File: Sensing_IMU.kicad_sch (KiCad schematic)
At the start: 7 parts, among them U3202 BMI270

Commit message: Finished layout, only cleaning left
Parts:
- TP3201: renamed from TP2807; value INT1 -> IMU_INT1
- TP3202: renamed from TP2808; value INT2 -> IMU_INT2
- renumbered C2805 to C3201, C2806 to C3202, R812 to R3201, R813 to R3202, U3202 to U3201
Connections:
- net INT1 is gone; now on net IMU_INT1: TP3201.1
- net INT2 is gone; now on net IMU_INT2: TP3202.1
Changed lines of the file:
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@@
 			"AAAAAAAAAAAAAAAAAAAAAAAAAAAAAAAAAAAAAAAAAAAAAAAAAAAAAAAAAAAAAAAAAAAAAAAAAAAA"
 			"AAAAAAAAAAAAAAAAAAAAAAAAAAAAAAAAAAAAAAAAAAAAAAAAAAAAAAAAAAAAAAAAAAAAAAAAAAAA"
-			"AAAAAAAAAAAAAAAAAAAAAAAAAAAAAAAAAAAAAAAAAAAAAAAAAAAAAAAAAAAAAA=="
+			"AAAAAAAAAAAAAAAAAAAAAAAAAAAAAAAAAAAAAAAAAAAAAAAAAAAAAAAAAAAAAEppbDVvaS9iQ0NS"
+			"ZjltNHVlaUYvRE9qN2tyNnFTb1JmMlpabWJRT1NmcXBkU0grVE5LbGJYWFBiTml3UVZhc1dDRk5U"
+			"VTFBQ1lnQTRpK2dzQ2cxTndIRVgyNkVEQkFEQWNSZkRDbG1Xd1BpTHh1M3ZMMFFmOWtKSXYreXN5"
+			"dTdKL0pQajdoTDZhY3FWT0p2M0xoeE1uSGlSTDJDQzJ3VjA2MitvVWsvRlN2aXI4RE5IZW5RWFBF"
+			"WGJyQ0l2M0N6bzNKekFvZy9jMmIwaUpBQTRpL0NVRFdYaFBqVEJHVzVHZUl2SDFEa1h6NStaZlpH"
+			"L3JWTjI3WDBVOVY5OFl0ZmxMRmp4eUwrMm83SzZOTVFwWjlhSU9MUEtHWWF2N2xudU9JdnpLMkEr"
+			"QXN6TjZyT1JnRHhsNDBidlNJamdQaUxMRkNENVNEK0RHQlpiSXI0eXc4VCtaZWZZVmtqSVAvcWsv"
+			"WkIrcW5LRUgvMTg4bDZObFRwcDlhTCtNdWFlcnI5dU9JdjNPd1JmK0ZtUitYbUJCQi81c3pvRVNF"
+			"QnhGK0VvV291Q2ZHbkNjcHlNOFNmSGFESVB6c2N5eGdGK2RlYXNpL1NUMVdseE44MTExd2preVpO"
+			"YWwya2czZWgzK29ic3ZSVGNTUCtIR3o2d0tkRS9JVWJJT0l2M095bzNKd0E0cytjR1QwaUpJRDRp"
+			"ekJVelNVaC9qUkJXVzZHK0xNSEZQbG5qMlhSSXlILzNpRHNrL1JURlgzcFMxK1NNV1BHSVA1eS9n"
+			"RUlYZnFwNVNQK2NtNkNCTHNqL3NJTkhmRVhiblpVYms0QThXZk9qQjRSRWtEOFJSaXE1cElRZjVx"
+			"Z0xEZEQvTmtGaXZ5enk3UEkwVktYZjc1SlA1VTE0aS8vam85Qitpa0tpTC84ZXlHMUVSQi80U2FP"
+			"K0FzM095bzNKNEQ0TTJkR2p3aWE5OHd1QUFBWXAwbEVRVlFKSVA0aURGVnpTWWcvVFZDV215SCtM"
+			"QVA5LzNESVAvdE1peG94VmZubm8vUlRHU3Z4ZC9YVlY4dmt5Wk9MaWx4NzNCQnY5ZDIxYTVlc1c3"
+			"ZE96ampqREprNmRhbzBOVFZwcjllM2hvZy8zeEx4dng3RW4vOFpOYW9ROGRlSURPZGpKSUQ0aXpG"
+			"VjFtUk1BUEZuakN5YURvZy9OMUVpL29yaGp2d3JobXNSbzZZbS8zeVZmaXBieEYvMkhSNlQ5Rk1V"
+			"RUgvWjkwS3FQUkYvNFNhUCtBczNPeW8zSjRENE0yZEdqd2dKSVA0aURGVnpTWWcvVFZDV215SCtM"
+			"QU50TVJ6eXJ3VU16dzlUa1g4K1N6KzFSWll2WHk1WFhYVVZWL3daL25sUjBtLwBhAAAASAAAAHUA"
+			"AABBAAAAWQAAAHgAAAAwAAAAawAAADMAAAB1AAAAawAAAGUAAABuAAAALwAAAGkAAABsAAAAMAAA"
+			"AHcAAABVAAAAdQAAADgAAABpAAAAagAAAFQAAABkAAAAVgAAAHcAAABGAAAAZgAAAG4AAABoAAAA"
+			"aAAAAGsAAAAvAAAAUwAAAGgAAABtAAAAcgAAAEgAAABMAAAANgAAAEkAAAA5AAAAdQAAAGoAAABJ"
+			"AAAARgAAAHoAAABNAAAAWAAAAFgAAABmAAAAbAAAAGUAAABrAAAAeAAAADkAAAB2AAAAaQAAAHAA"
+			"AABnAAAASwAAAFAAAABTAAAARgAAAGQAAABFAAAAMAAAAEYAAABYAAAAegAAAEgAAABUAAAAQQAA"
+			"ACsAAABhAAAAZgAAAGoAAABKAAAATgAAADIAAABNAAAAagAAAFkAAABMAAAAZAAAAE0AAAAyAAAA"
+			"dwAAAEEAAAA2AAAAZAAAAHAAAABOAAAAawAAAEcAAABEAAAASgAAAEEAAABOAAAAMwAAACsAAABq"
+			"AAAASwAAAFIAAAAxAAAANwAAADgAAABBAAAAVgAAAHcAAAB6AAAAaAAAAFIAAABxAAAAYgAAAEEA"
+			"AAB4AAAAcgAAAHcAAABvAAAATAAAADAAAABCAAAAQQAAAE0AAABCAAAASwAAAEIAAABNAAAAWgAA"
+			"ADYAAABJAAAAZwAAAG4AAAB3AAAAMAAAAEoAAABaAAAAawAAAEkAAABPAAAAYwAAAEEAAAAyAAAA"
+			"eAAAAG0AAABUAAAARwAAAHYAAABXAAAAaQAAAGEAAAA3AAAATAAAAHYAAABXAAAANAAAAGUAAABO"
+			"AAAAVQAAAHYAAABXAAAANwAAAFYAAABPAAAAbwAAAEYAAABTAAAASgAAAFgAAABEAAAARwAAAHoA"
+			"AABtAAAAMAAAADMAAAA5AAAASQAAAFUAAABDAAAAUwAAAHkAAABJAAAAZQAAADIAAABuAAAAQQAA"
+			"AG8AAABtAAAATwAAADYAAABzAAAALwAAAG4AAABOAAAAUgAAAE8AAAAzAAAAawAAAEkAAABWAAAA"
+			"VQAAADUAAAAzAAAAegAAAEIAAABqAAAANwAAADMAAABTAAAAQwAAAFgAAAAyAAAAQgAAAFEAAAAz"
+			"AAAAZAAAAHIAAABPAAAAWAAAAHQAAAB1AAAAaQAAAGoAAABUAAAAOQAAAHQAAABaAAAAegAAACsA"
+			"AAAyAAAATQAAAG4AAABiAAAAWAAAAEoAAABRAAAAQgAAACsAAABvAAAAcwAAAGYAAAAzAAAAdgAA"
+			"AHUAAAB3AAAAOQAAAHoAAABMAAAAQgAAAFAAAABnAAAARgAAADgAAAA3AAAAVw=="
 		)
 	)
@@
 		)
 	)
-	(label "INT2"
+	(label "IMU_INT2"
 		(at 22.86 97.79 0)
 		(effects
@@
 		)
 	)
-	(label "INT1"
+	(label "IMU_INT1"
 		(at 22.86 92.71 0)
 		(effects
@@
 		(on_board yes)
 		(dnp no)
-		(property "Reference" "R812"
+		(property "Reference" "R3201"
 			(at 118.618 86.868 0)
 			(effects
@@
 			(project "Plume"
 				(path "/0650c7a8-acba-429c-9f8e-eec0baf0bc1c/fede4c36-00cc-4d3d-b71c-5243ba232202/107f1a8c-fcbf-4d4a-9f6a-e2cb21670a9f"
-					(reference "R812")
+					(reference "R3201")
 					(unit 1)
 				)
@@
 		(dnp no)
 		(fields_autoplaced yes)
-		(property "Reference" "#PWR0706"
+		(property "Reference" "#PWR03202"
 			(at 154.94 93.98 0)
 			(effects
@@
 			(project "Plume"
 				(path "/0650c7a8-acba-429c-9f8e-eec0baf0bc1c/fede4c36-00cc-4d3d-b71c-5243ba232202/107f1a8c-fcbf-4d4a-9f6a-e2cb21670a9f"
-					(reference "#PWR0706")
+					(reference "#PWR03202")
 					(unit 1)
 				)
@@
 		(dnp no)
 		(fields_autoplaced yes)
-		(property "Reference" "#PWR0704"
+		(property "Reference" "#PWR03204"
 			(at 151.13 121.92 0)
 			(effects
@@
 			(project "Plume"
 				(path "/0650c7a8-acba-429c-9f8e-eec0baf0bc1c/fede4c36-00cc-4d3d-b71c-5243ba232202/107f1a8c-fcbf-4d4a-9f6a-e2cb21670a9f"
-					(reference "#PWR0704")
+					(reference "#PWR03204")
 					(unit 1)
 				)
@@
 		(on_board yes)
 		(dnp no)
-		(property "Reference" "TP2807"
+		(property "Reference" "TP3201"
 			(at 43.18 92.71 90)
 			(effects
@@
 			)
 		)
-		(property "Value" "INT1"
+		(property "Value" "IMU_INT1"
 			(at 50.546 92.71 90)
 			(effects
@@
 			(project "Plume"
 				(path "/0650c7a8-acba-429c-9f8e-eec0baf0bc1c/fede4c36-00cc-4d3d-b71c-5243ba232202/107f1a8c-fcbf-4d4a-9f6a-e2cb21670a9f"
-					(reference "TP2807")
+					(reference "TP3201")
 					(unit 1)
 				)
@@
 		(dnp no)
 		(fields_autoplaced yes)
-		(property "Reference" "#PWR0707"
+		(property "Reference" "#PWR03203"
 			(at 135.89 100.33 0)
 			(effects
@@
 			(project "Plume"
 				(path "/0650c7a8-acba-429c-9f8e-eec0baf0bc1c/fede4c36-00cc-4d3d-b71c-5243ba232202/107f1a8c-fcbf-4d4a-9f6a-e2cb21670a9f"
-					(reference "#PWR0707")
+					(reference "#PWR03203")
 					(unit 1)
 				)
@@
 		(dnp no)
 		(fields_autoplaced yes)
-		(property "Reference" "#PWR0705"
+		(property "Reference" "#PWR03201"
 			(at 147.32 93.98 0)
 			(effects
@@
 			(project "Plume"
 				(path "/0650c7a8-acba-429c-9f8e-eec0baf0bc1c/fede4c36-00cc-4d3d-b71c-5243ba232202/107f1a8c-fcbf-4d4a-9f6a-e2cb21670a9f"
-					(reference "#PWR0705")
+					(reference "#PWR03201")
 					(unit 1)
 				)
@@
 		(on_board yes)
 		(dnp no)
-		(property "Reference" "R813"
+		(property "Reference" "R3202"
 			(at 128.778 86.868 0)
 			(effects
@@
 			(project "Plume"
 				(path "/0650c7a8-acba-429c-9f8e-eec0baf0bc1c/fede4c36-00cc-4d3d-b71c-5243ba232202/107f1a8c-fcbf-4d4a-9f6a-e2cb21670a9f"
-					(reference "R813")
+					(reference "R3202")
 					(unit 1)
 				)
@@
 		(on_board yes)
 		(dnp no)
-		(property "Reference" "C2805"
+		(property "Reference" "C3201"
 			(at 144.78 82.55 0)
 			(effects
@@
 			(project "Plume"
 				(path "/0650c7a8-acba-429c-9f8e-eec0baf0bc1c/fede4c36-00cc-4d3d-b71c-5243ba232202/107f1a8c-fcbf-4d4a-9f6a-e2cb21670a9f"
-					(reference "C2805")
+					(reference "C3201")
 					(unit 1)
 				)
@@
 		(on_board yes)
 		(dnp no)
-		(property "Reference" "U3202"
+		(property "Reference" "U3201"
 			(at 142.494 92.71 0)
 			(effects
@@
 			(project ""
 				(path "/0650c7a8-acba-429c-9f8e-eec0baf0bc1c/fede4c36-00cc-4d3d-b71c-5243ba232202/107f1a8c-fcbf-4d4a-9f6a-e2cb21670a9f"
-					(reference "U3202")
+					(reference "U3201")
 					(unit 1)
 				)
@@
 		(on_board yes)
 		(dnp no)
-		(property "Reference" "TP2808"
+		(property "Reference" "TP3202"
 			(at 43.18 97.79 90)
 			(effects
@@
 			)
 		)
-		(property "Value" "INT2"
+		(property "Value" "IMU_INT2"
 			(at 50.546 97.79 90)
 			(effects
@@
 			(project "Plume"
 				(path "/0650c7a8-acba-429c-9f8e-eec0baf0bc1c/fede4c36-00cc-4d3d-b71c-5243ba232202/107f1a8c-fcbf-4d4a-9f6a-e2cb21670a9f"
-					(reference "TP2808")
+					(reference "TP3202")
 					(unit 1)
 				)
@@
 		(on_board yes)
 		(dnp no)
-		(property "Reference" "C2806"
+		(property "Reference" "C3202"
 			(at 157.48 82.55 0)
 			(effects
@@
 			(project "Plume"
 				(path "/0650c7a8-acba-429c-9f8e-eec0baf0bc1c/fede4c36-00cc-4d3d-b71c-5243ba232202/107f1a8c-fcbf-4d4a-9f6a-e2cb21670a9f"
-					(reference "C2806")
+					(reference "C3202")
 					(unit 1)
 				)

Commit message: Finished cleaning routing, removed errors, cleaned shematics, added pictures and other improvements
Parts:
- renumbered C3201 to C1001, C3202 to C1002, R3201 to R1001, R3202 to R1002, TP3201 to TP1001, TP3202 to TP1002, U3201 to U1001
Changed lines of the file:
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@@
 			"AAAAZAAAAHIAAABPAAAAWAAAAHQAAAB1AAAAaQAAAGoAAABUAAAAOQAAAHQAAABaAAAAegAAACsA"
 			"AAAyAAAATQAAAG4AAABiAAAAWAAAAEoAAABRAAAAQgAAACsAAABvAAAAcwAAAGYAAAAzAAAAdgAA"
-			"AHUAAAB3AAAAOQAAAHoAAABMAAAAQgAAAFAAAABnAAAARgAAADgAAAA3AAAAVw=="
+			"AHUAAAB3AAAAOQAAAHoAAABMAAAAQgAAAFAAAABnAAAARgAAADgAAAA3AAAAVwAAADcAAABLAAAA"
+			"cwAAAFEAAABqAAAAZwAAAGMAAABCAAAAQgAAAEIAAABBAAAAQQAAAEEAAABFAAAARQAAAEUAAABF"
+			"AAAAZwAAAG8AAABRAAAASgAAAHMAAABsAAAASQAAAFEAAABzAAAAVAAAAEUAAABVAAAAQQAAAEEA"
+			"AABBAAAAUQAAAFEAAABRAAAAUQAAAEEAAABBAAAAQgAAAEIAAABDAAAAcAAAAFoAAABJAAAATAAA"
+			"AFEAAAA3AAAAcQAAAHkAAAAyAAAAZwAAAHQAAABKAAAATAAAAFAAAABoAAAAOAAAADAAAABoAAAA"
+			"ZwAAAEEAAABBAAAAQwAAAEMAAABDAAAAQwAAAEEAAABBAAAAQQAAAEkAAABJAAAASQAAAEkAAABB"
+			"AAAAQQAAAEEAAABnAAAAZwAAAGcAAABnAAAAQQAAAEEAAABDAAAAQwAAAEMAAABDAAAAQQAAAEEA"
+			"AABBAAAASQAAAEkAAABJAAAASQAAAEEAAABBAAAAQQAAAGcAAABnAAAAZwAAAGcAAABBAAAAQQAA"
+			"AEMAAABDAAAAQwAAAEMAAABBAAAAQQAAAEEAAABJAAAASQAAAEkAAABJAAAAQQAAAEEAAABBAAAA"
+			"ZwAAAGcAAABnAAAAZwAAAEEAAABBAAAAQwAAAEMAAABGAAAAUgAAAFEAAABnAAAASQAAAEQAAABT"
+			"AAAAQwAAAHMAAABLAAAAeAAAAEcAAABnAAAASQAAAEkAAABJAAAASQAAAEEAAABBAAAAQQAAAGcA"
+			"AABnAAAAZwAAAGcAAABBAAAAQQAAAEMAAABDAAAAQwAAAEMAAABBAAAAQQAAAEEAAABJAAAASQAA"
+			"AEkAAABJAAAAQQAAAEEAAABBAAAAZwAAAGcAAABnAAAAZwAAAEEAAABBAAAAQwAAAEMAAABDAAAA"
+			"QwAAAEEAAABBAAAAQQAAAEkAAABJAAAASQAAAEkAAABBAAAAQQAAAEEAAABnAAAAZwAAAGcAAABn"
+			"AAAAQQAAAEEAAABDAAAAQwAAAEMAAABDAAAAQQAAAEEAAABBAAAASQAAAEkAAABJAAAASgAAAEEA"
+			"AAB2AAAAQQAAAHQAAABVAAAAVwAAAFUAAABMAAAAcgAAAE8AAABiAAAAOAAAAHYAAAB5AAAAeAAA"
+			"AFoAAABEAAAAegAAAFEAAABBAAAAQQAAAEIAAABCAAAARAAAAEkAAAB1AAAAOAAAAFAAAAAxAAAA"
+			"cQAAAE4AAABmAAAAdwAAACsAAAB1AAAASAAAAFoAAABtAAAAbgAAAEoAAABvAAAAZAAAAEkAAABJ"
+			"AAAAQQAAAEEAAABBAAAAZwAAAGcAAABnAAAAZwAAAEEAAABBAAAAQwAAAEMAAA=="
 		)
 	)
@@
 		(on_board yes)
 		(dnp no)
-		(property "Reference" "R3201"
+		(property "Reference" "R1001"
 			(at 118.618 86.868 0)
 			(effects
@@
 			(project "Plume"
 				(path "/0650c7a8-acba-429c-9f8e-eec0baf0bc1c/fede4c36-00cc-4d3d-b71c-5243ba232202/107f1a8c-fcbf-4d4a-9f6a-e2cb21670a9f"
-					(reference "R3201")
+					(reference "R1001")
 					(unit 1)
 				)
@@
 		(dnp no)
 		(fields_autoplaced yes)
-		(property "Reference" "#PWR03202"
+		(property "Reference" "#PWR01002"
 			(at 154.94 93.98 0)
 			(effects
@@
 			(project "Plume"
 				(path "/0650c7a8-acba-429c-9f8e-eec0baf0bc1c/fede4c36-00cc-4d3d-b71c-5243ba232202/107f1a8c-fcbf-4d4a-9f6a-e2cb21670a9f"
-					(reference "#PWR03202")
+					(reference "#PWR01002")
 					(unit 1)
 				)
@@
 		(dnp no)
 		(fields_autoplaced yes)
-		(property "Reference" "#PWR03204"
+		(property "Reference" "#PWR01004"
 			(at 151.13 121.92 0)
 			(effects
@@
 			(project "Plume"
 				(path "/0650c7a8-acba-429c-9f8e-eec0baf0bc1c/fede4c36-00cc-4d3d-b71c-5243ba232202/107f1a8c-fcbf-4d4a-9f6a-e2cb21670a9f"
-					(reference "#PWR03204")
+					(reference "#PWR01004")
 					(unit 1)
 				)
@@
 		(on_board yes)
 		(dnp no)
-		(property "Reference" "TP3201"
+		(property "Reference" "TP1001"
 			(at 43.18 92.71 90)
 			(effects
@@
 			(project "Plume"
 				(path "/0650c7a8-acba-429c-9f8e-eec0baf0bc1c/fede4c36-00cc-4d3d-b71c-5243ba232202/107f1a8c-fcbf-4d4a-9f6a-e2cb21670a9f"
-					(reference "TP3201")
+					(reference "TP1001")
 					(unit 1)
 				)
@@
 		(dnp no)
 		(fields_autoplaced yes)
-		(property "Reference" "#PWR03203"
+		(property "Reference" "#PWR01003"
 			(at 135.89 100.33 0)
 			(effects
@@
 			(project "Plume"
 				(path "/0650c7a8-acba-429c-9f8e-eec0baf0bc1c/fede4c36-00cc-4d3d-b71c-5243ba232202/107f1a8c-fcbf-4d4a-9f6a-e2cb21670a9f"
-					(reference "#PWR03203")
+					(reference "#PWR01003")
 					(unit 1)
 				)
@@
 		(dnp no)
 		(fields_autoplaced yes)
-		(property "Reference" "#PWR03201"
+		(property "Reference" "#PWR01001"
 			(at 147.32 93.98 0)
 			(effects
@@
 			(project "Plume"
 				(path "/0650c7a8-acba-429c-9f8e-eec0baf0bc1c/fede4c36-00cc-4d3d-b71c-5243ba232202/107f1a8c-fcbf-4d4a-9f6a-e2cb21670a9f"
-					(reference "#PWR03201")
+					(reference "#PWR01001")
 					(unit 1)
 				)
@@
 		(on_board yes)
 		(dnp no)
-		(property "Reference" "R3202"
+		(property "Reference" "R1002"
 			(at 128.778 86.868 0)
 			(effects
@@
 			(project "Plume"
 				(path "/0650c7a8-acba-429c-9f8e-eec0baf0bc1c/fede4c36-00cc-4d3d-b71c-5243ba232202/107f1a8c-fcbf-4d4a-9f6a-e2cb21670a9f"
-					(reference "R3202")
+					(reference "R1002")
 					(unit 1)
 				)
@@
 		(on_board yes)
 		(dnp no)
-		(property "Reference" "C3201"
+		(property "Reference" "C1001"
 			(at 144.78 82.55 0)
 			(effects
@@
 			(project "Plume"
 				(path "/0650c7a8-acba-429c-9f8e-eec0baf0bc1c/fede4c36-00cc-4d3d-b71c-5243ba232202/107f1a8c-fcbf-4d4a-9f6a-e2cb21670a9f"
-					(reference "C3201")
+					(reference "C1001")
 					(unit 1)
 				)
@@
 		(on_board yes)
 		(dnp no)
-		(property "Reference" "U3201"
+		(property "Reference" "U1001"
 			(at 142.494 92.71 0)
 			(effects
@@
 			(project ""
 				(path "/0650c7a8-acba-429c-9f8e-eec0baf0bc1c/fede4c36-00cc-4d3d-b71c-5243ba232202/107f1a8c-fcbf-4d4a-9f6a-e2cb21670a9f"
-					(reference "U3201")
+					(reference "U1001")
 					(unit 1)
 				)
@@
 		(on_board yes)
 		(dnp no)
-		(property "Reference" "TP3202"
+		(property "Reference" "TP1002"
 			(at 43.18 97.79 90)
 			(effects
@@
 			(project "Plume"
 				(path "/0650c7a8-acba-429c-9f8e-eec0baf0bc1c/fede4c36-00cc-4d3d-b71c-5243ba232202/107f1a8c-fcbf-4d4a-9f6a-e2cb21670a9f"
-					(reference "TP3202")
+					(reference "TP1002")
 					(unit 1)
 				)
@@
 		(on_board yes)
 		(dnp no)
-		(property "Reference" "C3202"
+		(property "Reference" "C1002"
 			(at 157.48 82.55 0)
 			(effects
@@
 			(project "Plume"
 				(path "/0650c7a8-acba-429c-9f8e-eec0baf0bc1c/fede4c36-00cc-4d3d-b71c-5243ba232202/107f1a8c-fcbf-4d4a-9f6a-e2cb21670a9f"
-					(reference "C3202")
+					(reference "C1002")
 					(unit 1)
 				)

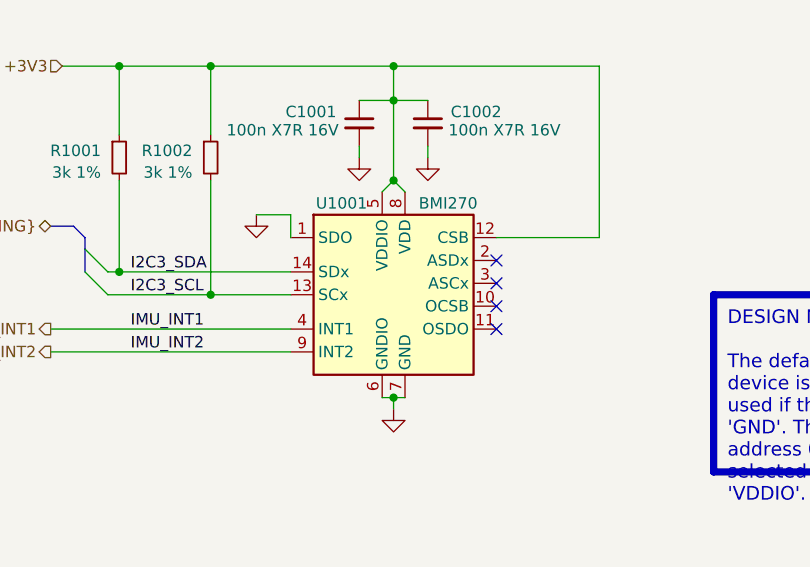
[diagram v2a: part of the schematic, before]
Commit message: Added PCB frame
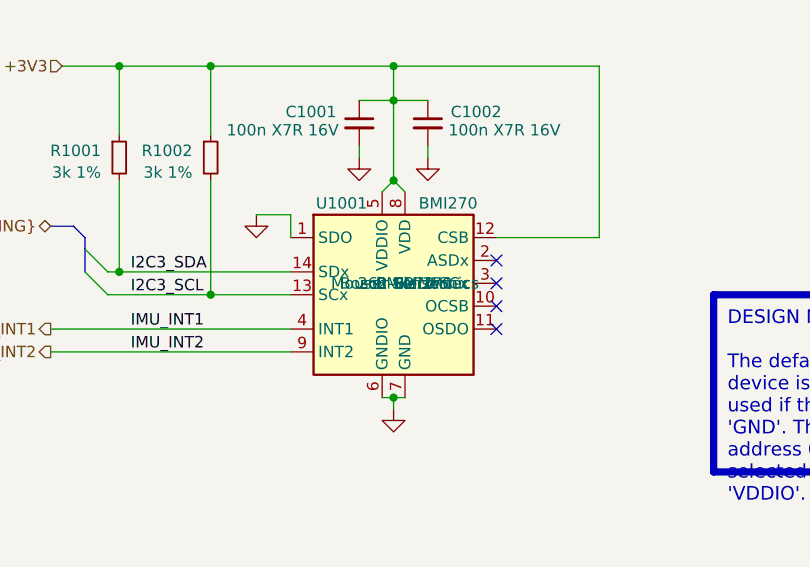
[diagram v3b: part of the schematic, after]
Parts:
- U1001: Manufacturer (none) -> Bosch Sensortec; Manufacturer Part Number (none) -> BMI270; Supplier (none) -> Mouser Electronics; Supplier Part Number (none) -> 262-BMI270
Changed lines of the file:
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@@
 			"AFoAAABEAAAAegAAAFEAAABBAAAAQQAAAEIAAABCAAAARAAAAEkAAAB1AAAAOAAAAFAAAAAxAAAA"
 			"cQAAAE4AAABmAAAAdwAAACsAAAB1AAAASAAAAFoAAABtAAAAbgAAAEoAAABvAAAAZAAAAEkAAABJ"
-			"AAAAQQAAAEEAAABBAAAAZwAAAGcAAABnAAAAZwAAAEEAAABBAAAAQwAAAEMAAA=="
+			"AAAAQQAAAEEAAABBAAAAZwAAAGcAAABnAAAAZwAAAEEAAABBAAAAQwAAAEMAAAAAAAAAAAAAAAAA"
+			"AAAAAAAAAAAAAAAAAAAAAAAAAAAAAAAAAAAAAAAAAAAAAAAAAAAAAAAAAAAAAAAAAAAAAAAAAAAA"
+			"AAAAAAAAAAAAAAAAAAAAAAAAAAAAAAAAAAAAAAAAAAAAAAAAAAAAAAAAAAAAAAAAAAAAAAAAAAAA"
+			"AAAAAAAAAAAAAAAAAAAAAAAAAAAAAAAAAAAAAAAAAAAAAAAAAAAAAAAAAAAAAAAAAAAAAAAAAAAA"
+			"AAAAAAAAAAAAAAAAAAAAAAAAAAAAAAAAAAAAAAAAAAAAAAAAAAAAAAAAAAAAAAAAAAAAAAAAAAAA"
+			"AAAAAAAAAAAAAAAAAAAAAAAAAAAAAAAAAAAAAAAAAAAAAAAAAAAAAAAAAAAAAAAAAAAAAAAAAAAA"
+			"AAAAAAAAAAAAAAAAAAAAAAAAAAAAAAAAAAAAAAAAAAAAAAAAAAAAAAAAAAAAAAAAAAAAAAAAAAAA"
+			"AAAAAAAAAAAAAAAAAAAAAAAAAAAAAAAAAAAAAAAAAAAAAAAAAAAAAAAAAAAAAAAAAAAAAAAAAAAA"
+			"AAAAAAAAAAAAAAAAAAAAAAAAAAAAAAAAAAAAAAAAAAAAAAAAAAAAAAAAAAAAAAAAAAAAAAAAAAAA"
+			"AAAAAAAAAAAAAAAAAAAAAAAAAAAAAAAAAAAAAAAAAAAAAAAAAAAAAAAAAAAAAAAAAAAAAAAAAAAA"
+			"AAAAAAAAAAAAAAAAAAAAAAAAAAAAAAAAAAAAAAAAAAAAAAAAAAAAAAAAAAAAAAAAAAAAAAAAAAAA"
+			"AAAAAAAAAAAAAAAAAAAAAAAAAAAAAAAAAAAAAAAAAAAAAAAAAAAAAAAAAAAAAAAAAAAAAAAAAAAA"
+			"AAAAAAAAAAAAAAAAAAAAAAAAAAAAAAAAAAAAAAAAAAAAAAAAAAAAAAAAAAAAAAAAAAAAAAAAAAAA"
+			"AAAAAAAAAAAAAAAAAAAAAAAAAAAAAAAAAAAAAAAAAAAAAAAAAAAAAAAAAAAAAAAAAAAAAAAAAAAA"
+			"AAAAAAAAAAAAAAAAAAAAAAAAAAAAAAAAAAAAAAAAAAAAAAAAAAAAAAAAAAAAAAAAAAAAAAAAAAAA"
+			"AAAAAAAAAAAAAAAAAAAAAAAAAAAAAAAAAAAAAAAAAAAAAAAAAAAAAAAAAAAAAAAAAAAAAAAAAAAA"
+			"AAAAAAAAAAAAAAAAAAAAAAAAAAAAAAAAAAAAAAAAAAAAAAAAAAAAAAAAAAAAAAAAAAAAAAAAAAAA"
+			"AAAAAAAAAAAAAAAAAAAAAAAAAAAAAAAAAAAAAAAAAAAAAAAAAAAAAAAAAAAAAAAAAAAAAAAAAAAA"
+			"AAAAAAAAAAAAAAAAAAAAAAAAAAAAAAAAAAAAAAAAAAAAAAAAAAAAAAAAAAAAAAAAADgAAABGAAAA"
+			"NAAAAFcAAABNAAAANwAAAGIAAABLAAAAagAAADYAAABVAAAAUQAAAGYAAABhAAAATwAAAFoAAAAy"
+			"AAAAQgAAACsAAAAwAAAAcAAAAGsAAAB4AAAAUQAAAGQAAABkAAAATgAAAEQAAABxAAAAYQAAAHQA"
+			"AAA3AAAALwAAAGkAAAB4AAAARQAAAFYAAABIAAAAMgAAAHkAAABiAAAAYQAAAEQAAAA2AAAAQQAA"
+			"AFMAAAB1AAAAZQAAAFAAAAB3AAAAUgAAAFgAAABnAAAAOAAAAHQAAABhAAAATgAAAEQAAAA4AAAA"
+			"awAAAGEAAAA3AAAAMAAAAEoAAABkAAAASAAAAHYAAABhAAAAWQAAADYAAAA5AAAAagAAAGYAAAAz"
+			"AAAATwAAAEUAAABNAAAATwAAAG0AAABpAAAAegAAAEEAAABnAAAAYgAAAHIAAABVAAAANwAAAFQA"
+			"AAA1AAAAbgAAAGoAAABSAAAALwAAAGEAAABkAAAAWQAAADYAAABlAAAAZQAAADgAAABrAAAANgAA"
+			"AGUAAABxAAAATgAAAEgAAABkAAAAUAAAAFgAAAB4AAAAYQAAAGEAAAB2AAAAbwAAAFYAAAAvAAAA"
+			"MAAAAGMAAAB5AAAAVAAAAG8AAABnAAAAYgAAAFkAAABDAAAATwAAAGYAAABCAAAAeQAAAHUAAAA0"
+			"AAAAOQAAAG8AAAB6AAAAMAAAAE4AAABPAAAAMwAAAHkAAAB2AAAAQgAAAE4AAABaAAAAcAAAAEUA"
+			"AABLAAAANQAAAGQAAABqAAAAaQAAADkAAABoAAAAbQAAAHQAAABoAAAAMQAAADkAAAByAAAAMwAA"
+			"AGUAAABoAAAATAAAACsAAAA2AAAASAAAAEYAAAB1AAAAWQAAAHQAAABzAAAAUwAAAFQAAABNAAAA"
+			"ZQAAAEcAAABTAAAAdgAAAEcAAAAyAAAAZgAAAFYAAABUAAAAQQAAAFgAAABSAAAAegAAAHYAAABO"
+			"AAAAZAAAAG8AAABnAAAAagAAAFkAAABVAAAAMQAAAGUAAABIAAAAcwAAADIAAAA0AAAAYgAAAGgA"
+			"AABJAAAAYwAAAEEAAABWAAAAZgAAAFgAAABLAAAAegAAAEQAAAAzAAAAWQAAAHcAAAAwAAAAWgAA"
+			"ADcAAABVAAAAdwAAAGMAAABFAAAAYgAAAHEAAAArAAAAZwAAAEYAAAArAAAATwAAAE0AAAA0AAAA"
+			"TwAAAFYAAABOAAAAMAAAAEYAAABzAAAAQwAAAHAAAABnAAAANAAAADcAAABrAAAASQAAAHgAAAB2"
+			"AAAAKwAAAGcAAABRAAAAaAAAADYAAAA0AAAARQAAAHoAAABSAAAARwAAAGoAAA=="
 		)
 	)
@@
 			)
 		)
+		(property "Manufacturer" "Bosch Sensortec"
+			(at 152.4 101.6 0)
+			(effects
+				(font
+					(size 1.27 1.27)
+				)
+			)
+		)
+		(property "Manufacturer Part Number" "BMI270"
+			(at 152.4 101.6 0)
+			(effects
+				(font
+					(size 1.27 1.27)
+				)
+			)
+		)
+		(property "Supplier" "Mouser Electronics"
+			(at 152.4 101.6 0)
+			(effects
+				(font
+					(size 1.27 1.27)
+				)
+			)
+		)
+		(property "Supplier Part Number" "262-BMI270"
+			(at 152.4 101.6 0)
+			(effects
+				(font
+					(size 1.27 1.27)
+				)
+			)
+		)
